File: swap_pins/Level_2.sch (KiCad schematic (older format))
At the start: 6 parts, among them U301 PIC18F452-IP

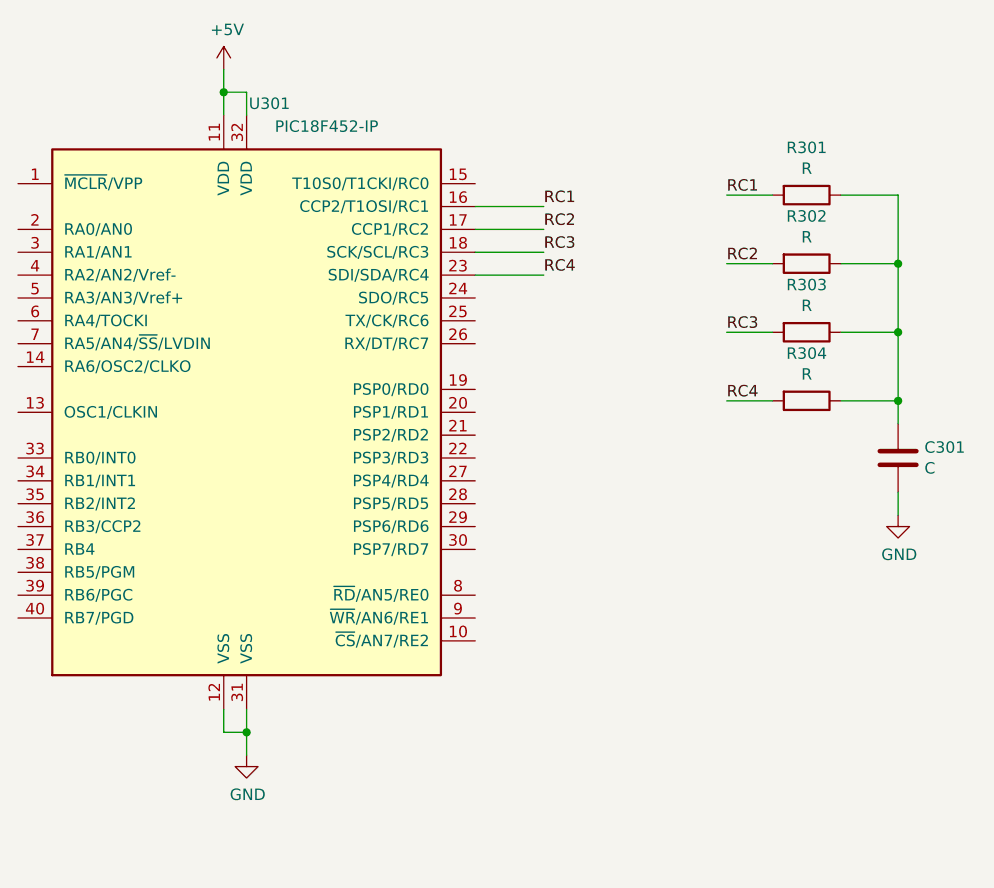
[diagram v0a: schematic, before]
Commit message: added global label test
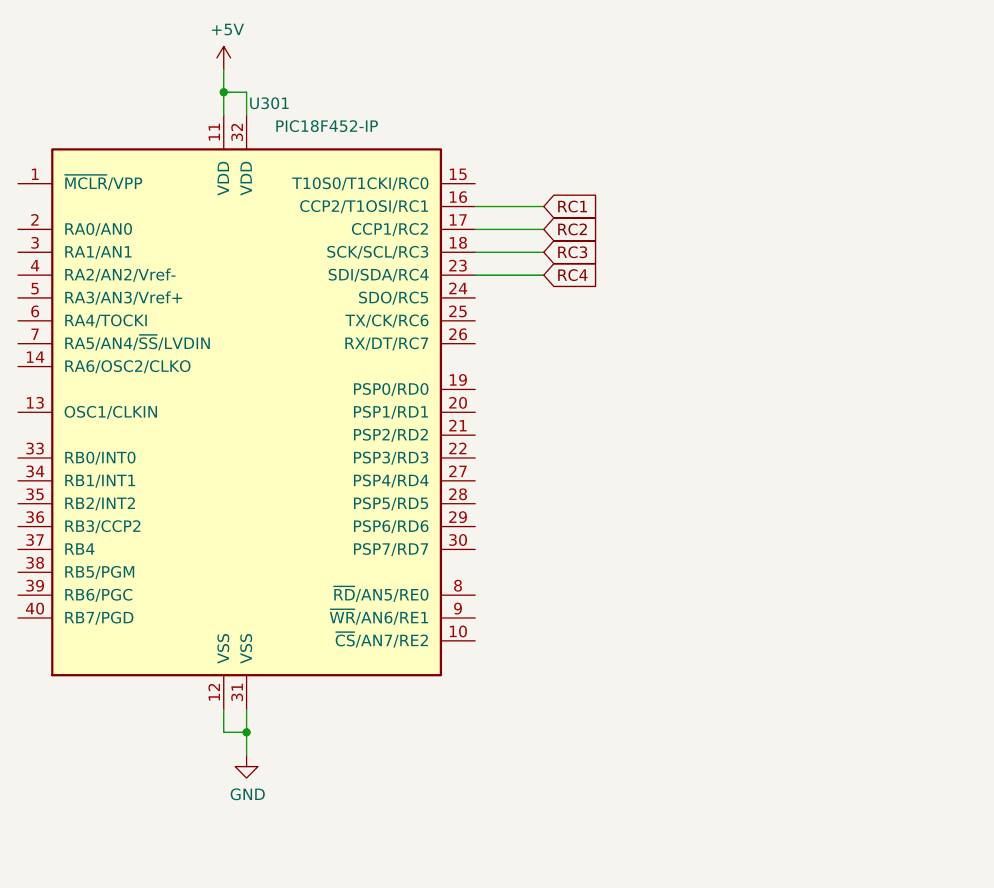
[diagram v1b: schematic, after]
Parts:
- removed C301: C, Capacitor_THT:C_Disc_D7.5mm_W5.0mm_P5.00mm, symbol Device:C
- removed R301, R302, R303, R304: R, Resistor_THT:R_Axial_DIN0614_L14.3mm_D5.7mm_P20.32mm_Horizontal, symbol Device:R
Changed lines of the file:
@@
 EESchema Schematic File Version 4
+LIBS:swap_pins_test-cache
 EELAYER 26 0
 EELAYER END
@@
 Wire Wire Line
 	4200 3200 4500 3200
-Text Label 4500 2900 0    50   ~ 0
-RC1
-Text Label 4500 3000 0    50   ~ 0
-RC2
-Text Label 4500 3100 0    50   ~ 0
-RC3
-Text Label 4500 3200 0    50   ~ 0
-RC4
-$Comp
-L Device:R R301
-U 1 1 5B293C65
-P 5650 2850
-F 0 "R301" V 5443 2850 50  0000 C CNN
-F 1 "R" V 5534 2850 50  0000 C CNN
-F 2 "Resistor_THT:R_Axial_DIN0614_L14.3mm_D5.7mm_P20.32mm_Horizontal" V 5580 2850 50  0001 C CNN
-F 3 "~" H 5650 2850 50  0001 C CNN
-	1    5650 2850
-	0    1    1    0
-$EndComp
-$Comp
-L Device:R R302
-U 1 1 5B293D9F
-P 5650 3150
-F 0 "R302" V 5443 3150 50  0000 C CNN
-F 1 "R" V 5534 3150 50  0000 C CNN
-F 2 "Resistor_THT:R_Axial_DIN0614_L14.3mm_D5.7mm_P20.32mm_Horizontal" V 5580 3150 50  0001 C CNN
-F 3 "~" H 5650 3150 50  0001 C CNN
-	1    5650 3150
-	0    1    1    0
-$EndComp
-$Comp
-L Device:R R303
-U 1 1 5B293DBD
-P 5650 3450
-F 0 "R303" V 5443 3450 50  0000 C CNN
-F 1 "R" V 5534 3450 50  0000 C CNN
-F 2 "Resistor_THT:R_Axial_DIN0614_L14.3mm_D5.7mm_P20.32mm_Horizontal" V 5580 3450 50  0001 C CNN
-F 3 "~" H 5650 3450 50  0001 C CNN
-	1    5650 3450
-	0    1    1    0
-$EndComp
-$Comp
-L Device:R R304
-U 1 1 5B293DDD
-P 5650 3750
-F 0 "R304" V 5443 3750 50  0000 C CNN
-F 1 "R" V 5534 3750 50  0000 C CNN
-F 2 "Resistor_THT:R_Axial_DIN0614_L14.3mm_D5.7mm_P20.32mm_Horizontal" V 5580 3750 50  0001 C CNN
-F 3 "~" H 5650 3750 50  0001 C CNN
-	1    5650 3750
-	0    1    1    0
-$EndComp
-$Comp
-L Device:C C301
-U 1 1 5B293E54
-P 6050 4000
-F 0 "C301" H 6165 4046 50  0000 L CNN
-F 1 "C" H 6165 3955 50  0000 L CNN
-F 2 "Capacitor_THT:C_Disc_D7.5mm_W5.0mm_P5.00mm" H 6088 3850 50  0001 C CNN
-F 3 "~" H 6050 4000 50  0001 C CNN
-	1    6050 4000
-	1    0    0    -1
-$EndComp
-Wire Wire Line
-	5500 2850 5300 2850
-Wire Wire Line
-	5500 3150 5300 3150
-Wire Wire Line
-	5500 3450 5300 3450
-Wire Wire Line
-	5500 3750 5300 3750
-Wire Wire Line
-	5800 3750 6050 3750
-Wire Wire Line
-	6050 3750 6050 3850
-Wire Wire Line
-	5800 3450 6050 3450
-Wire Wire Line
-	6050 3450 6050 3750
-Connection ~ 6050 3750
-Wire Wire Line
-	5800 3150 6050 3150
-Wire Wire Line
-	6050 3150 6050 3450
-Connection ~ 6050 3450
-Wire Wire Line
-	5800 2850 6050 2850
-Wire Wire Line
-	6050 2850 6050 3150
-Connection ~ 6050 3150
-Text Label 5300 2850 0    50   ~ 0
-RC1
-Text Label 5300 3150 0    50   ~ 0
-RC2
-Text Label 5300 3450 0    50   ~ 0
-RC3
-Text Label 5300 3750 0    50   ~ 0
-RC4
-$Comp
-L power:GND #PWR0303
-U 1 1 5B294318
-P 6050 4250
-F 0 "#PWR0303" H 6050 4000 50  0001 C CNN
-F 1 "GND" H 6055 4077 50  0000 C CNN
-F 2 "" H 6050 4250 50  0001 C CNN
-F 3 "" H 6050 4250 50  0001 C CNN
-	1    6050 4250
-	1    0    0    -1
-$EndComp
-Wire Wire Line
-	6050 4250 6050 4150
 Wire Wire Line
 	3100 5100 3100 5200
@@
 	1    0    0    -1
 $EndComp
+Text GLabel 4500 2900 2    50   Input ~ 0
+RC1
+Text GLabel 4500 3000 2    50   Input ~ 0
+RC2
+Text GLabel 4500 3100 2    50   Input ~ 0
+RC3
+Text GLabel 4500 3200 2    50   Input ~ 0
+RC4
 $EndSCHEMATC

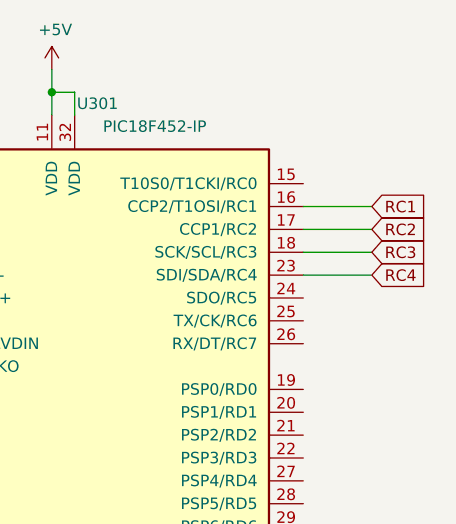
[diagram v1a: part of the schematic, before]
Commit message: changed project to include hierarchical labels also
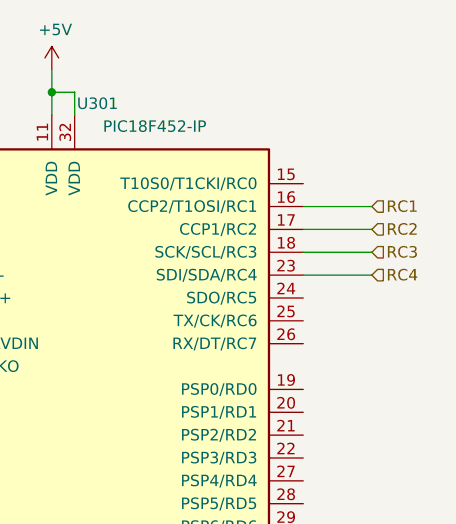
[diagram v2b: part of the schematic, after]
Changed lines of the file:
@@
 	1    0    0    -1
 $EndComp
-Text GLabel 4500 2900 2    50   Input ~ 0
+Text HLabel 4500 2900 2    50   Input ~ 0
 RC1
-Text GLabel 4500 3000 2    50   Input ~ 0
+Text HLabel 4500 3000 2    50   Input ~ 0
 RC2
-Text GLabel 4500 3100 2    50   Input ~ 0
+Text HLabel 4500 3100 2    50   Input ~ 0
 RC3
-Text GLabel 4500 3200 2    50   Input ~ 0
+Text HLabel 4500 3200 2    50   Input ~ 0
 RC4
 $EndSCHEMATC

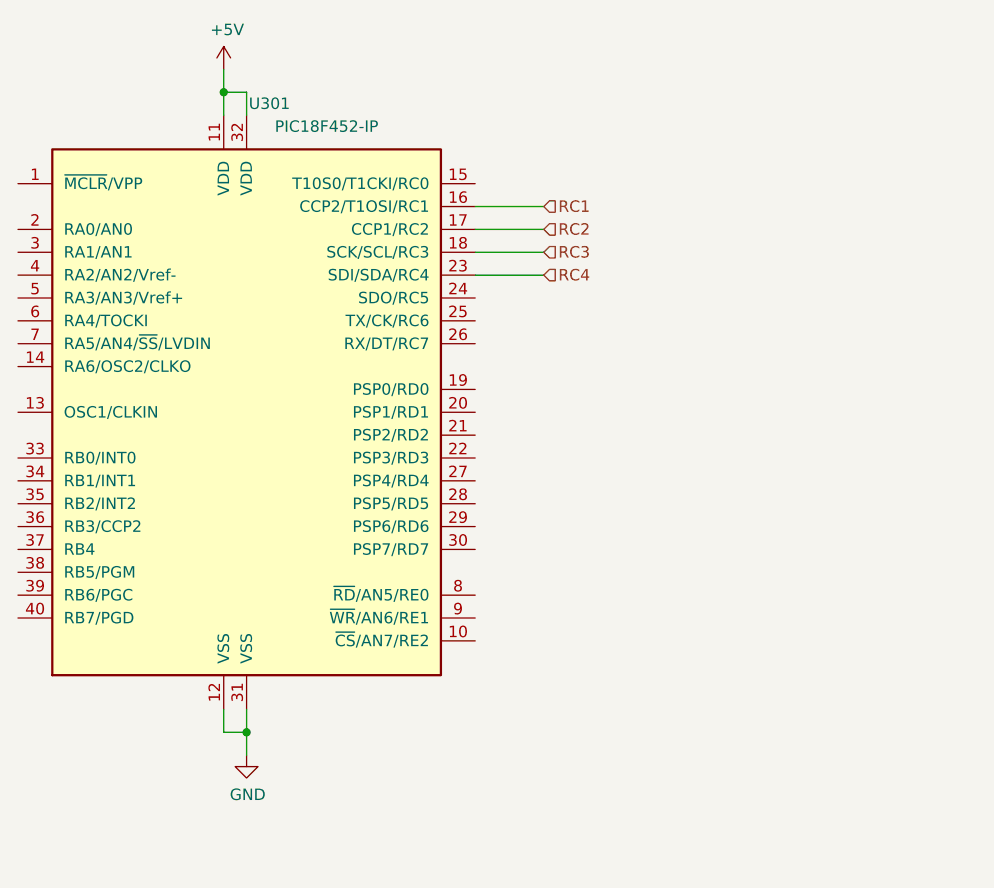
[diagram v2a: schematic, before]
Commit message: Overwritten the plugin with V2 version
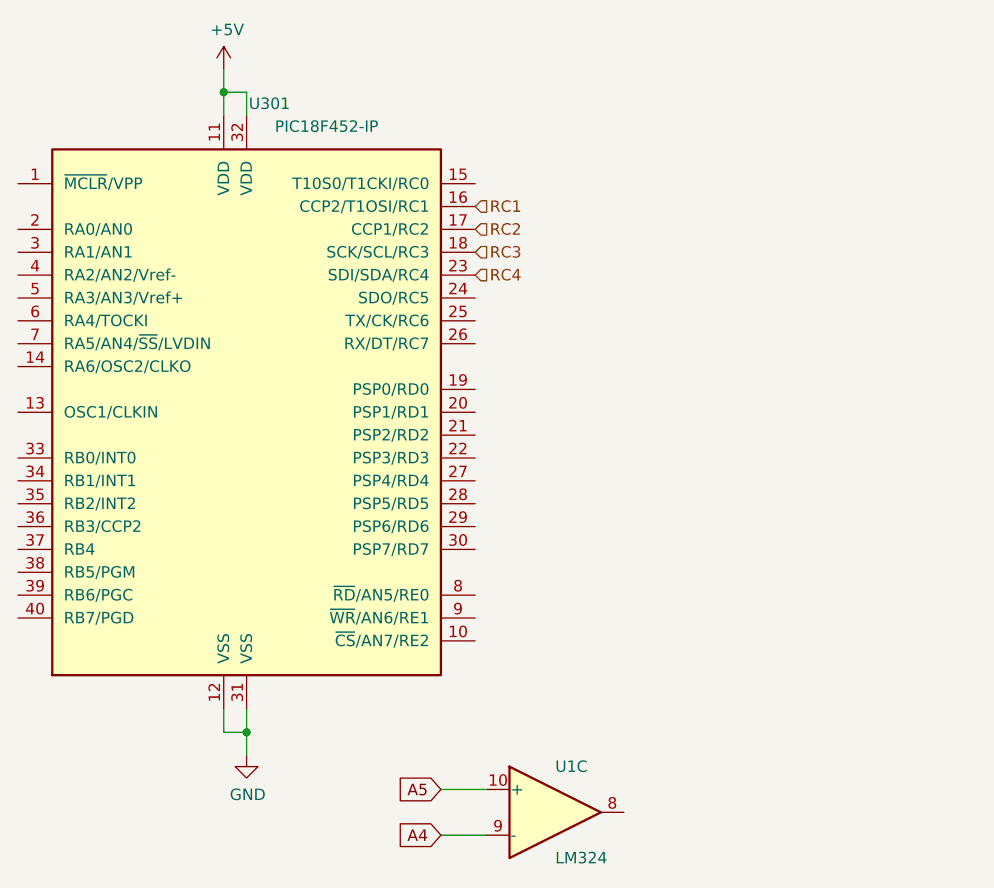
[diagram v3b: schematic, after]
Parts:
- added U1: LM324, symbol Amplifier_Operational:LM324
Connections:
- new net A4: U1.9 (-)
- new net A5: U1.10 (+)
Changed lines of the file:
@@
 $EndComp
-Wire Wire Line
-	4200 2900 4500 2900
-Wire Wire Line
-	4200 3000 4500 3000
-Wire Wire Line
-	4200 3100 4500 3100
-Wire Wire Line
-	4200 3200 4500 3200
 Wire Wire Line
 	3100 5100 3100 5200
@@
 	1    0    0    -1
 $EndComp
-Text HLabel 4500 2900 2    50   Input ~ 0
+Text HLabel 4200 2900 2    50   Input ~ 0
 RC1
-Text HLabel 4500 3000 2    50   Input ~ 0
+Text HLabel 4200 3000 2    50   Input ~ 0
 RC2
-Text HLabel 4500 3100 2    50   Input ~ 0
+Text HLabel 4200 3100 2    50   Input ~ 0
 RC3
-Text HLabel 4500 3200 2    50   Input ~ 0
+Text HLabel 4200 3200 2    50   Input ~ 0
 RC4
+$Comp
+L Amplifier_Operational:LM324 U1
+U 3 1 5B34BA87
+P 4550 5550
+F 0 "U1" H 4550 5750 50  0000 L CNN
+F 1 "LM324" H 4550 5350 50  0000 L CNN
+F 2 "" H 4500 5650 50  0001 C CNN
+F 3 "http://www.ti.com/lit/ds/symlink/lm2902-n.pdf" H 4600 5750 50  0001 C CNN
+	3    4550 5550
+	1    0    0    -1
+$EndComp
+Wire Wire Line
+	4250 5650 4050 5650
+Text GLabel 4050 5650 0    50   Input ~ 0
+A4
+Wire Wire Line
+	4250 5450 4050 5450
+Text GLabel 4050 5450 0    50   Input ~ 0
+A5
 $EndSCHEMATC
